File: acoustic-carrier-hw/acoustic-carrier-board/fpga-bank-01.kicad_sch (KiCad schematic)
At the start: 22 parts, among them IC1 ECP5-BGA256

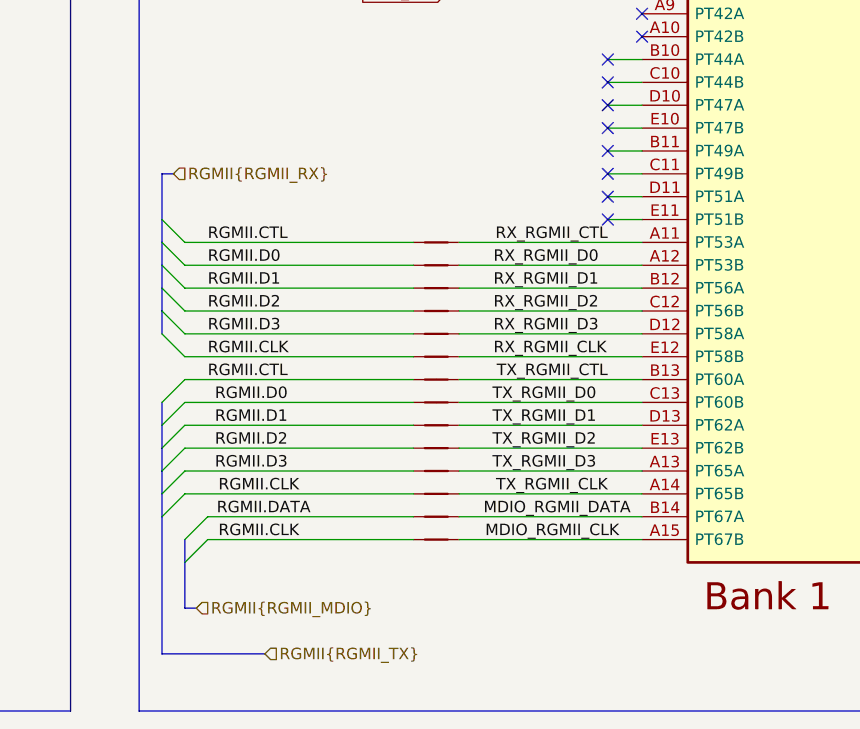
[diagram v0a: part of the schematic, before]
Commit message: [carrier] Removed USB-switch, placed decouplpling for DDR3 and ECP5U (next) consider adding buffers on CC1 and CC2 pins
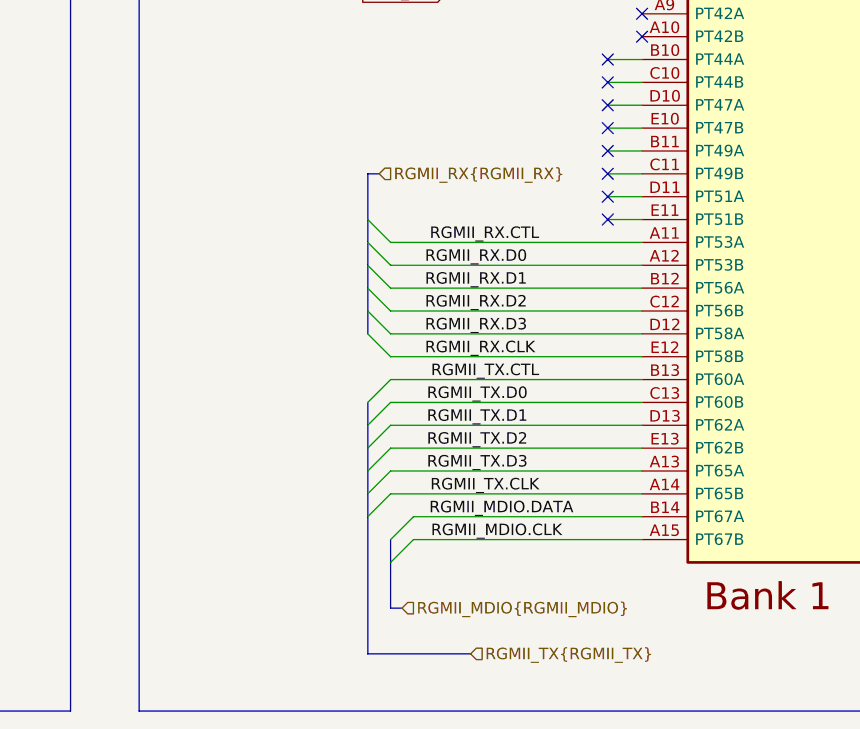
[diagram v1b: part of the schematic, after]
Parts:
- removed NT401, NT402, NT403, NT404, NT405, NT406, NT407, NT408, NT409, NT410, NT415, NT416, NT417, NT418: NetTie_2, iw-misc:NetTie-2_SMD_Pad0.1565mm, symbol Device:NetTie_2
- C401, C402, C404, C405: footprint Capacitor_SMD:C_0402_1005Metric -> Capacitor_SMD:C_0201_0603Metric; LPN C307331 -> C22435929; MPN CL05B104KB54PNC -> CGA0201X7R104K160ET
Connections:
- net MDIO_RGMII_CLK renamed RGMII_MDIO.CLK
- net MDIO_RGMII_DATA renamed RGMII_MDIO.DATA
- net RX_RGMII_CLK renamed RGMII_RX.CLK
- net RX_RGMII_CTL renamed RGMII_RX.CTL
- net RX_RGMII_D0 renamed RGMII_RX.D0
- net RX_RGMII_D1 renamed RGMII_RX.D1
- net RX_RGMII_D2 renamed RGMII_RX.D2
- net RX_RGMII_D3 renamed RGMII_RX.D3
- net TX_RGMII_CLK renamed RGMII_TX.CLK
- net TX_RGMII_CTL renamed RGMII_TX.CTL
- net TX_RGMII_D0 renamed RGMII_TX.D0
- net TX_RGMII_D1 renamed RGMII_TX.D1
- net TX_RGMII_D2 renamed RGMII_TX.D2
- net TX_RGMII_D3 renamed RGMII_TX.D3

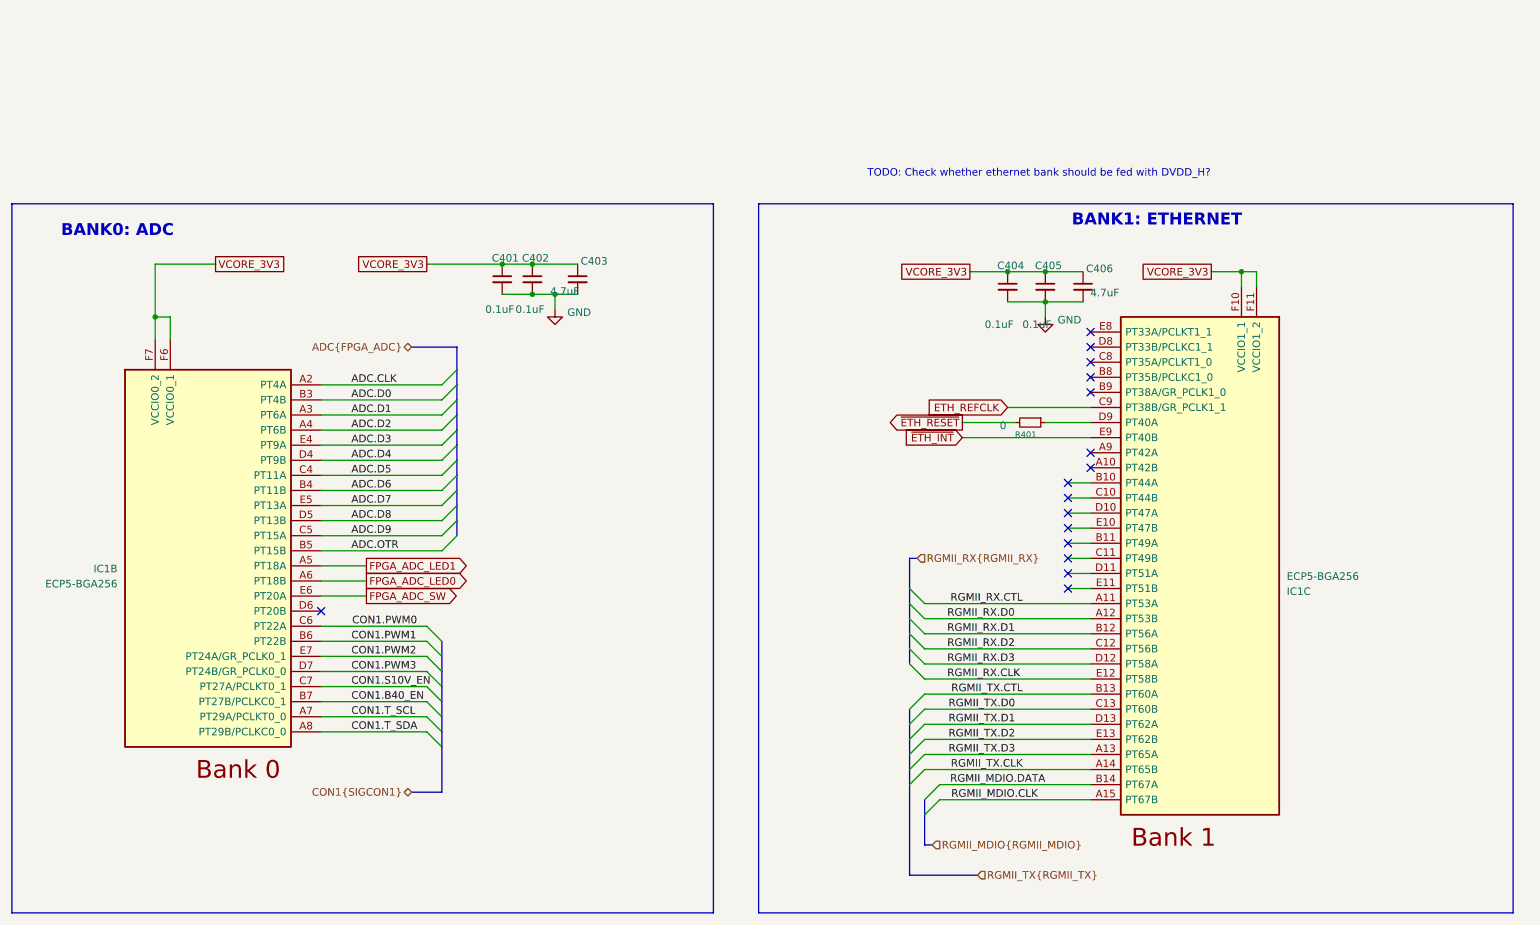
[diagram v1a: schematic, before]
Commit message: [carrier] connected ethernet, usb and adc to appropriate banks, redpositioned schmitt trigger and USB
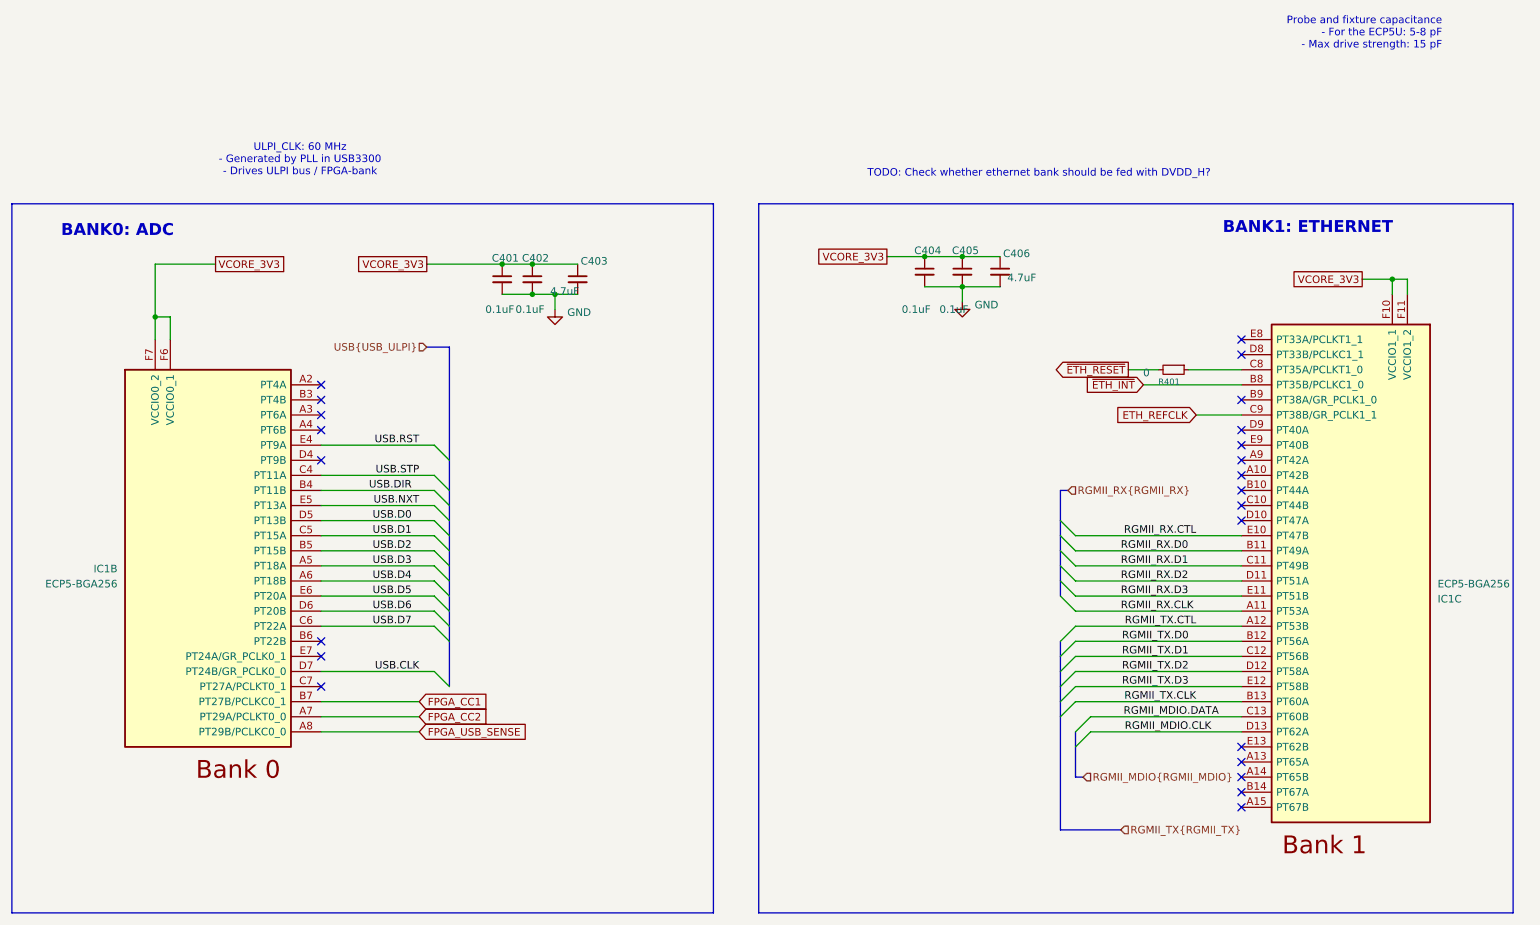
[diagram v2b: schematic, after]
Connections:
- net RGMII_MDIO.CLK: now also IC1.D13 (PT62A); no longer IC1.A15 (PT67B)
- net RGMII_MDIO.DATA: now also IC1.C13 (PT60B); no longer IC1.B14 (PT67A)
- net RGMII_RX.CLK: now also IC1.A11 (PT53A); no longer IC1.E12 (PT58B)
- net RGMII_RX.CTL: now also IC1.E10 (PT47B); no longer IC1.A11 (PT53A)
- net RGMII_RX.D0: now also IC1.B11 (PT49A); no longer IC1.A12 (PT53B)
- net RGMII_RX.D1: now also IC1.C11 (PT49B); no longer IC1.B12 (PT56A)
- net RGMII_RX.D2: now also IC1.D11 (PT51A); no longer IC1.C12 (PT56B)
- net RGMII_RX.D3: now also IC1.E11 (PT51B); no longer IC1.D12 (PT58A)
- net RGMII_TX.CLK: now also IC1.B13 (PT60A); no longer IC1.A14 (PT65B)
- net RGMII_TX.CTL: now also IC1.A12 (PT53B); no longer IC1.B13 (PT60A)
- net RGMII_TX.D0: now also IC1.B12 (PT56A); no longer IC1.C13 (PT60B)
- net RGMII_TX.D1: now also IC1.C12 (PT56B); no longer IC1.D13 (PT62A)
- net RGMII_TX.D2: now also IC1.D12 (PT58A); no longer IC1.E13 (PT62B)
- net RGMII_TX.D3: now also IC1.E12 (PT58B); no longer IC1.A13 (PT65A)
- net ~{ETH_INT}: now also IC1.B8 (PT35B/PCLKC1_0); no longer IC1.E9 (PT40B)
- net at IC1.C8 (PT35A/PCLKT1_0): now also R401.1
- net at IC1.D9 (PT40A): no longer R401.1
- net USB.D6: now reaches IC1.D6 (PT20B)
- net ADC.CLK: no longer names the net of IC1.A2 (PT4A)
- net ADC.D0: no longer names the net of IC1.B3 (PT4B)
- net ADC.D1: no longer names the net of IC1.A3 (PT6A)
- net ADC.D2: no longer names the net of IC1.A4 (PT6B)
- net ADC.D3 renamed USB.RST
- net ADC.D4: no longer names the net of IC1.D4 (PT9B)
- net ADC.D5 renamed USB.STP
- net ADC.D6 renamed USB.DIR
- net ADC.D7 renamed USB.NXT
- net ADC.D8 renamed USB.D0
- net ADC.D9 renamed USB.D1
- net ADC.OTR renamed USB.D2
- net CON1.B40_EN renamed FPGA_CC1
- net CON1.PWM0 renamed USB.D7
- net CON1.PWM1: no longer names the net of IC1.B6 (PT22B)
- net CON1.PWM2: no longer names the net of IC1.E7 (PT24A/GR_PCLK0_1)
- net CON1.PWM3 renamed USB.CLK
- net CON1.S10V_EN: no longer names the net of IC1.C7 (PT27A/PCLKT0_1)
- net CON1.T_SCL renamed FPGA_CC2
- net CON1.T_SDA renamed FPGA_USB_SENSE
- net FPGA_ADC_LED0 renamed USB.D4
- net FPGA_ADC_LED1 renamed USB.D3
- net FPGA_ADC_SW renamed USB.D5
- no-connect marks 16 -> 23
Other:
- note added: "Probe and fixture capacitance - For the ECP5U: 5-8 pF - Max drive strength: 15 pF"
- note added: "ULPI_CLK: 60 MHz - Generated by PLL in USB3300 - Drives ULPI bus / FPGA-bank"
- moved on the sheet: C404, C405, C406, IC1C

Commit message: [¢arrier] Placed power supply circuitry appropraitely, changed power connector (next) Place schmitt triggers between usb and power, put critical circuitry closer together, place config circuitry
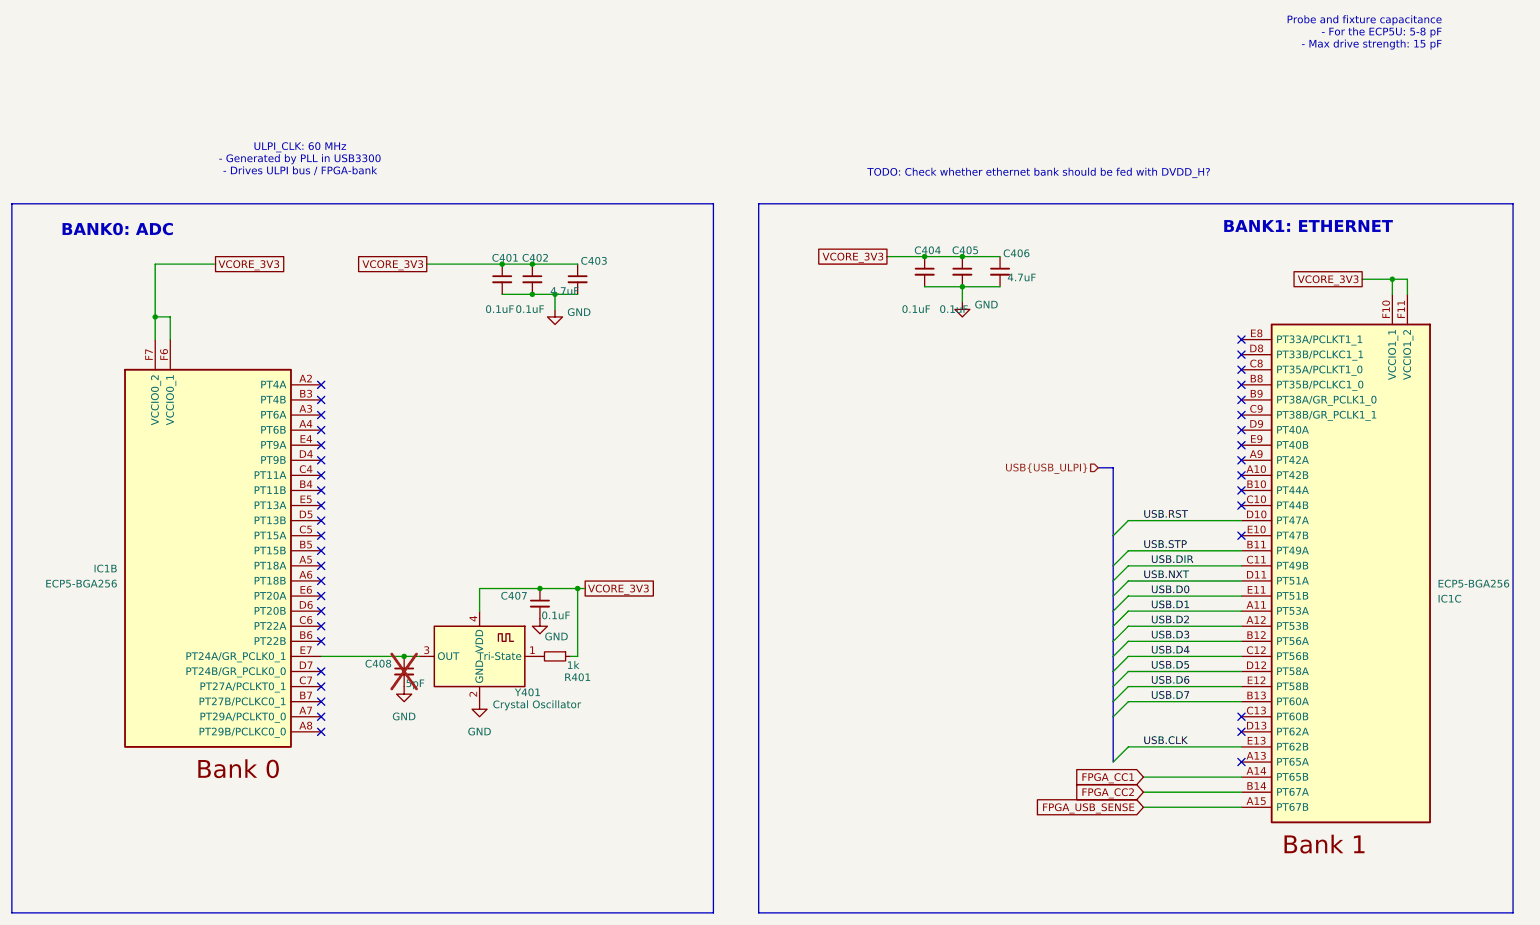
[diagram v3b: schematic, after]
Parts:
- added C407: 0.1uF, Capacitor_SMD:C_0201_0603Metric, symbol Device:C_Small
- added C408: 5pF, Capacitor_SMD:C_0603_1608Metric, symbol Device:C_Small
- added Y401: Crystal Oscillator, Crystal:Crystal_SMD_3225-4Pin_3.2x2.5mm, symbol Oscillator:ASCO
- R401: value 0 -> 1k; LPN C21189 -> C21190; MPN 0603WAF0000T5E -> 0603WAF1001T5E
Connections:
- net RGMII_RX.CLK is gone; now on net USB.D1: IC1.A11 (PT53A)
- net RGMII_RX.D0 is gone; now on net USB.STP: IC1.B11 (PT49A)
- net RGMII_RX.D1 is gone; now on net USB.DIR: IC1.C11 (PT49B)
- net RGMII_RX.D2 is gone; now on net USB.NXT: IC1.D11 (PT51A)
- net RGMII_RX.D3 is gone; now on net USB.D0: IC1.E11 (PT51B)
- net RGMII_TX.CLK is gone; now on net USB.D7: IC1.B13 (PT60A)
- net RGMII_TX.CTL is gone; now on net USB.D2: IC1.A12 (PT53B)
- net RGMII_TX.D0 is gone; now on net USB.D3: IC1.B12 (PT56A)
- net RGMII_TX.D1 is gone; now on net USB.D4: IC1.C12 (PT56B)
- net RGMII_TX.D2 is gone; now on net USB.D5: IC1.D12 (PT58A)
- net RGMII_TX.D3 is gone; now on net USB.D6: IC1.E12 (PT58B)
- net FPGA_CC1: now also IC1.A14 (PT65B); no longer IC1.B7 (PT27B/PCLKC0_1)
- net FPGA_CC2: now also IC1.B14 (PT67A); no longer IC1.A7 (PT29A/PCLKT0_0)
- net FPGA_USB_SENSE: now also IC1.A15 (PT67B); no longer IC1.A8 (PT29B/PCLKC0_0)
- net GND: now also C407.2, C408.2, Y401.2 (GND)
- net USB.CLK: now also IC1.E13 (PT62B); no longer IC1.D7 (PT24B/GR_PCLK0_0)
- net USB.D0: no longer IC1.D5 (PT13B)
- net USB.D1: no longer IC1.C5 (PT15A)
- net USB.D2: no longer IC1.B5 (PT15B)
- net USB.D3: no longer IC1.A5 (PT18A)
- net USB.D4: no longer IC1.A6 (PT18B)
- net USB.D5: no longer IC1.E6 (PT20A)
- net USB.D6: no longer IC1.D6 (PT20B)
- net USB.D7: no longer IC1.C6 (PT22A)
- net USB.DIR: no longer IC1.B4 (PT11B)
- net USB.NXT: no longer IC1.E5 (PT13A)
- net USB.RST: now also IC1.D10 (PT47A); no longer IC1.E4 (PT9A)
- net USB.STP: no longer IC1.C4 (PT11A)
- net VCORE_3V3: now also R401.1, C407.1, Y401.4 (VDD)
- net at IC1.C8 (PT35A/PCLKT1_0): no longer R401.1
- net at IC1.E7 (PT24A/GR_PCLK0_1): now also C408.1, Y401.3 (OUT)
- net ETH_REFCLK: no longer names the net of IC1.C9 (PT38B/GR_PCLK1_1)
- net RGMII_MDIO.CLK: no longer names the net of IC1.D13 (PT62A)
- net RGMII_MDIO.DATA: no longer names the net of IC1.C13 (PT60B)
- net RGMII_RX.CTL: no longer names the net of IC1.E10 (PT47B)
- net ~{ETH_INT}: no longer names the net of IC1.B8 (PT35B/PCLKC1_0)
- net ~{ETH_RESET}: no longer names the net of R401.2
- net ~{ETH_RESET}: now also Y401.1 (Tri-State)
- no-connect marks 23 -> 39
